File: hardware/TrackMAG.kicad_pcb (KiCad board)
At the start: 4 copper layers, 36 x 36 mm, 57 parts, among them J1 USB_C_Socket_USB2.0, J2 Conn_Debug, SW1 SW_RESET, SW2 SW_BOOT, SW3 SW_CALIBRATE, U1 LSM6DS3TR-C, U2 USBLC6-2P6, U3 STM32F103C8T6, U4 LIS2MDL, U5 AMS1117-3.3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

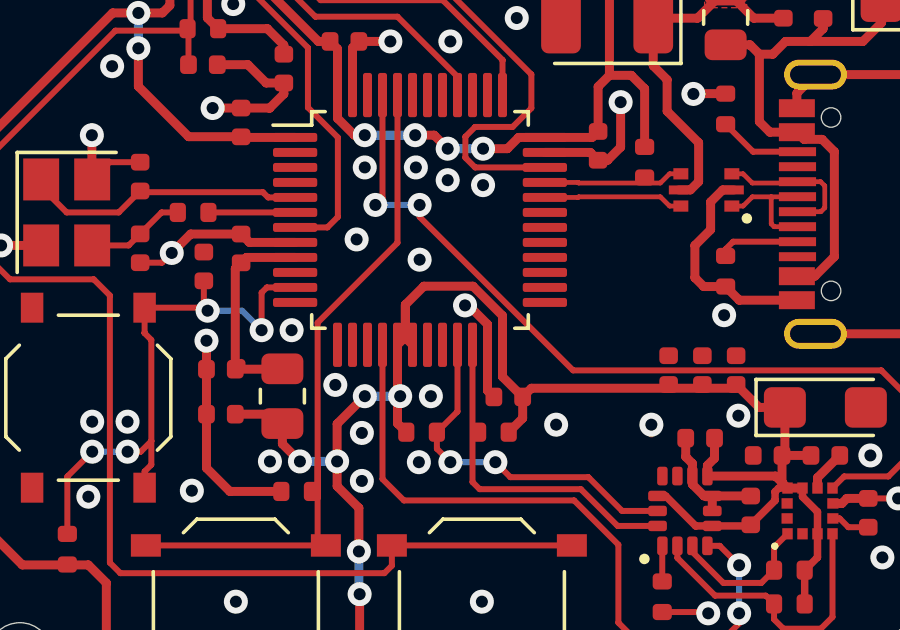
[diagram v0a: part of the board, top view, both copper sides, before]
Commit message: Remove redundant connection on PB0
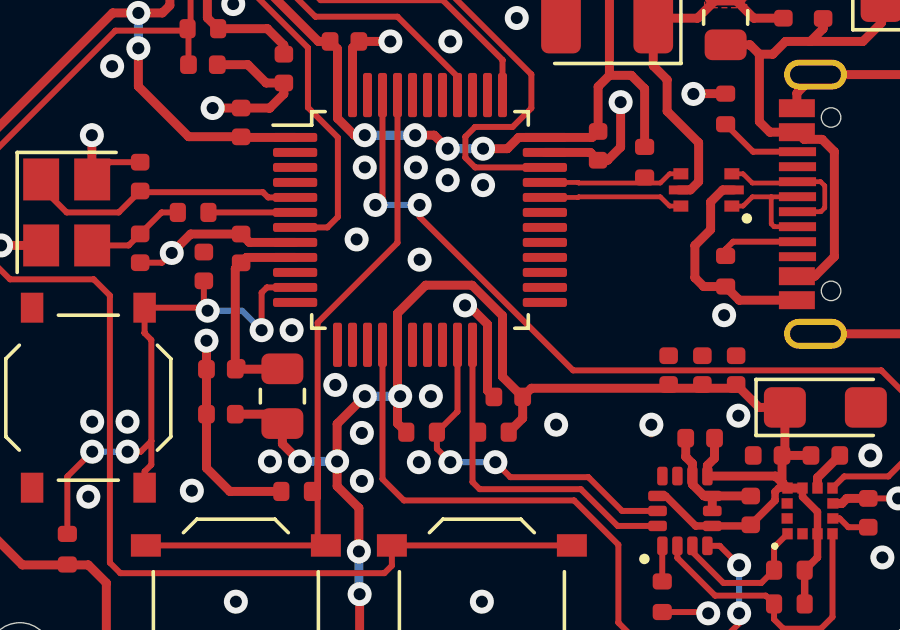
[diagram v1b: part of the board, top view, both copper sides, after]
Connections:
- U3 pad 18: +3.3V -> unconnected-(U3-PB0-Pad18)
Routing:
- net +3.3V: track 186.9 -> 185.5 mm
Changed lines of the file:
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@@
   (net 58 "/U_D+")
   (net 59 "/U_D-")
+  (net 60 "unconnected-(U3-PB0-Pad18)")
   (footprint "TrackMAG:C_0402_1005Metric" (layer "F.Cu")
     (at 148.725 97.375 180)
@@
       (net 1 "+3.3V") (pinfunction "PA7") (pintype "bidirectional"))
     (pad "18" smd roundrect (at -0.25 4.1625) (size 0.3 1.475) (layers "F.Cu" "F.Paste" "F.Mask") (roundrect_rratio 0.25)
-      (net 1 "+3.3V") (pinfunction "PB0") (pintype "bidirectional"))
+      (net 60 "unconnected-(U3-PB0-Pad18)") (pinfunction "PB0") (pintype "bidirectional+no_connect"))
     (pad "19" smd roundrect (at 0.25 4.1625) (size 0.3 1.475) (layers "F.Cu" "F.Paste" "F.Mask") (roundrect_rratio 0.25)
       (net 32 "unconnected-(U3-PB1-Pad19)") (pinfunction "PB1") (pintype "bidirectional+no_connect"))
@@
   (segment (start 127.675 71.675) (end 129.325 71.675) (width 0.3) (layer "F.Cu") (net 1))
   (segment (start 134.3875 83.8225) (end 134.14 83.575) (width 0.3) (layer "F.Cu") (net 1))
-  (segment (start 136.65 93.425) (end 136.3875 93.6875) (width 0.3) (layer "F.Cu") (net 1))
   (segment (start 146.955 97.47) (end 146.955 96.8) (width 0.3) (layer "F.Cu") (net 1))
   (segment (start 133.75 83.575) (end 129.325 79.15) (width 0.3) (layer "F.Cu") (net 1))
@@
   (segment (start 149.095 98.4625) (end 149.3875 98.4625) (width 0.25) (layer "F.Cu") (net 1))
   (segment (start 130.05 81.675) (end 130.05 82.79) (width 0.3) (layer "F.Cu") (net 1))
+  (segment (start 137.325 91.7) (end 138.870335 91.7) (width 0.3) (layer "F.Cu") (net 1))
   (segment (start 127.75 83.8045) (end 127.75 85.075) (width 0.3) (layer "F.Cu") (net 1))
   (segment (start 150.3875 99.9875) (end 150.3875 100.7725) (width 0.25) (layer "F.Cu") (net 1))
   (segment (start 146.88 99.725) (end 148.125 99.725) (width 0.25) (layer "F.Cu") (net 1))
   (segment (start 139.8875 93.6875) (end 139.8875 92.717165) (width 0.3) (layer "F.Cu") (net 1))
-  (segment (start 137.266685 91.733315) (end 136.65 92.35) (width 0.3) (layer "F.Cu") (net 1))
   (segment (start 141.3 86.775) (end 140.425 86.775) (width 0.3) (layer "F.Cu") (net 1))
-  (segment (start 139.8875 92.717165) (end 138.90365 91.733315) (width 0.3) (layer "F.Cu") (net 1))
+  (segment (start 138.870335 91.7) (end 139.8875 92.717165) (width 0.3) (layer "F.Cu") (net 1))
   (segment (start 127.75 82.625) (end 128.55 82.625) (width 0.3) (layer "F.Cu") (net 1))
   (segment (start 149.3 97.28) (end 149.205 97.375) (width 0.3) (layer "F.Cu") (net 1))
@@
   (segment (start 130.05 82.79) (end 130.41 83.15) (width 0.3) (layer "F.Cu") (net 1))
   (segment (start 143.4525 81.285) (end 140.7825 81.285) (width 0.3) (layer "F.Cu") (net 1))
+  (segment (start 136.3875 93.6875) (end 136.3875 92.6375) (width 0.3) (layer "F.Cu") (net 1))
   (segment (start 134.3875 86.1375) (end 134.949305 86.699305) (width 0.3) (layer "F.Cu") (net 1))
   (segment (start 134.85 104.125) (end 134 104.125) (width 0.3) (layer "F.Cu") (net 1))
@@
   (segment (start 146.7175 97.7075) (end 146.955 97.47) (width 0.3) (layer "F.Cu") (net 1))
   (segment (start 126.8305 72.5195) (end 127.675 71.675) (width 0.3) (layer "F.Cu") (net 1))
-  (segment (start 136.65 93.45) (end 136.8875 93.6875) (width 0.3) (layer "F.Cu") (net 1))
   (segment (start 148.44 95.775) (end 147.675 95.01) (width 0.3) (layer "F.Cu") (net 1))
   (segment (start 140.56 95.425) (end 140.56 96.135) (width 0.3) (layer "F.Cu") (net 1))
   (segment (start 150.3875 99.9875) (end 150.3875 99.255) (width 0.25) (layer "F.Cu") (net 1))
   (segment (start 149.205 97.375) (end 150.17 97.375) (width 0.3) (layer "F.Cu") (net 1))
-  (segment (start 136.65 92.35) (end 136.65 93.45) (width 0.3) (layer "F.Cu") (net 1))
   (segment (start 150.3875 99.255) (end 149.8875 98.755) (width 0.25) (layer "F.Cu") (net 1))
-  (segment (start 138.90365 91.733315) (end 137.266685 91.733315) (width 0.3) (layer "F.Cu") (net 1))
   (segment (start 132.05 83.15) (end 130.41 83.15) (width 0.3) (layer "F.Cu") (net 1))
   (segment (start 131.17 86.75) (end 131.175 86.755) (width 0.3) (layer "F.Cu") (net 1))
@@
   (segment (start 131.195 86.775) (end 131.175 86.755) (width 0.3) (layer "F.Cu") (net 1))
   (segment (start 149.3875 98.4625) (end 149.8875 98.4625) (width 0.3) (layer "F.Cu") (net 1))
-  (segment (start 136.65 92.35) (end 136.65 93.425) (width 0.3) (layer "F.Cu") (net 1))
   (segment (start 143.075 85.0825) (end 143.4525 84.705) (width 0.3) (layer "F.Cu") (net 1))
   (segment (start 127.75 82.625) (end 126.8925 82.625) (width 0.3) (layer "F.Cu") (net 1))
@@
   (segment (start 140.425 86.775) (end 140.05 87.15) (width 0.3) (layer "F.Cu") (net 1))
   (segment (start 140.05 87.15) (end 139.2395 87.15) (width 0.3) (layer "F.Cu") (net 1))
+  (segment (start 136.3875 92.6375) (end 137.325 91.7) (width 0.3) (layer "F.Cu") (net 1))
   (segment (start 132.2375 96) (end 132.55 96.3125) (width 0.3) (layer "F.Cu") (net 1))
   (segment (start 136.675 96.595) (end 136.68 96.6) (width 0.2) (layer "F.Cu") (net 1))

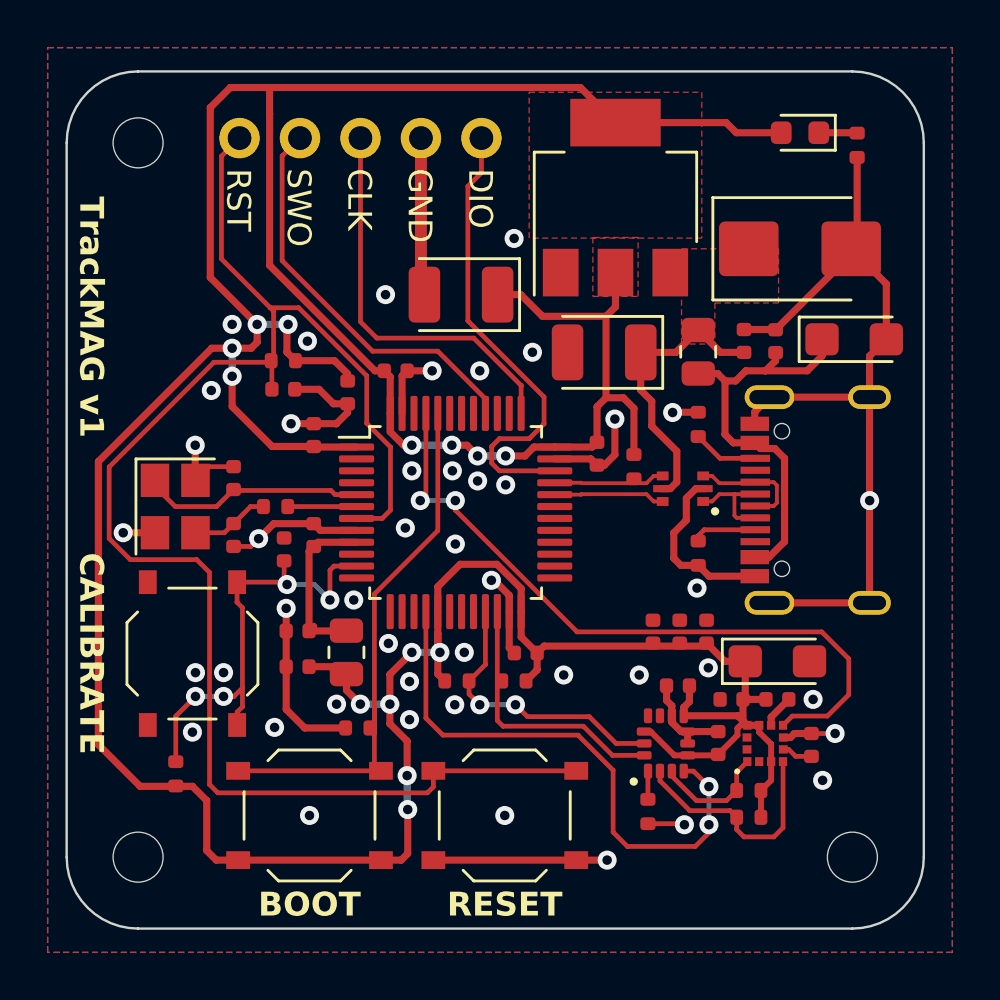
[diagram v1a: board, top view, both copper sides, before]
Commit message: Remove redundant vias, adjust reference vias
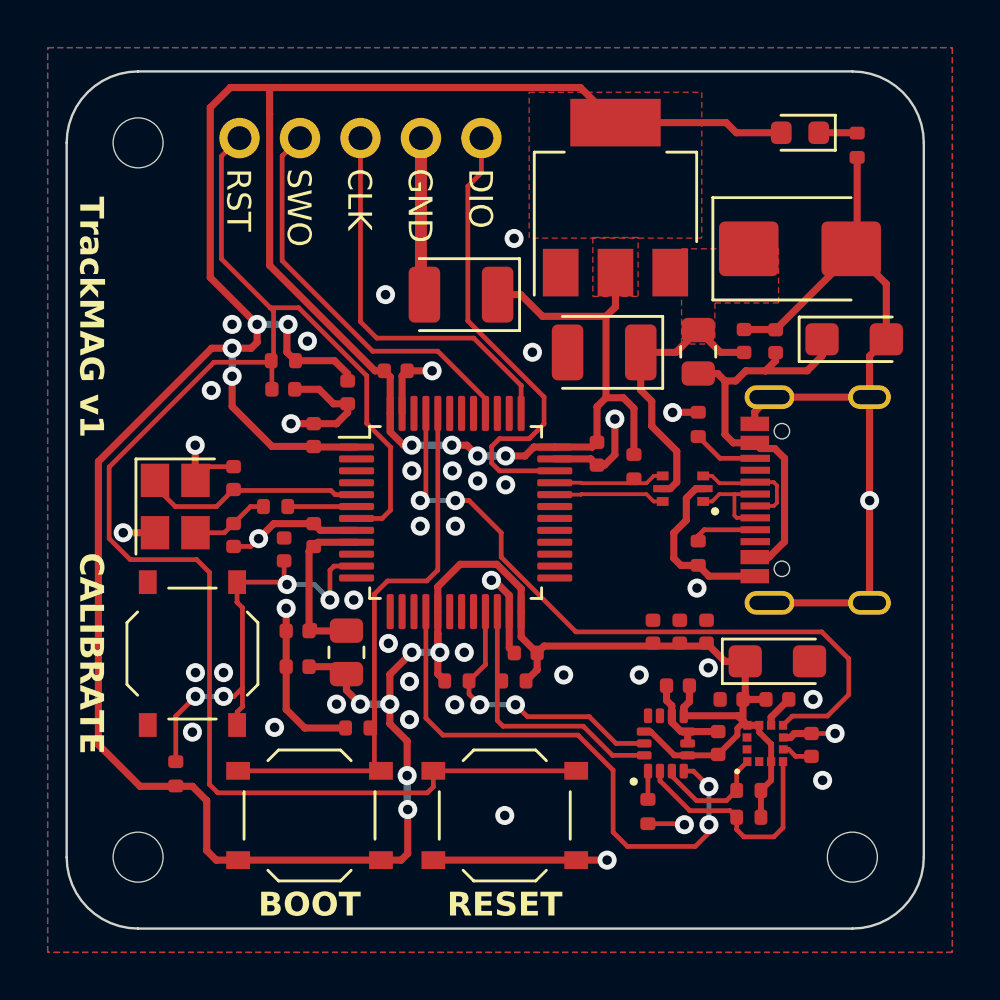
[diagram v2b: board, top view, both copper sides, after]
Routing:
- net /BOOT0: track 23.5 -> 24.5 mm
- net GND: vias 45 -> 43
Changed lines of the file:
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@@
   (via (at 152.15 97.375) (size 0.8) (drill 0.4) (layers "F.Cu" "B.Cu") (net 2))
   (via (at 134.1925 80.375) (size 0.8) (drill 0.4) (layers "F.Cu" "B.Cu") (free) (net 2))
-  (via (at 138.15 83.575) (size 0.8) (drill 0.4) (layers "F.Cu" "B.Cu") (free) (net 2))
   (via (at 135.296271 87.775) (size 0.8) (drill 0.4) (layers "F.Cu" "B.Cu") (free) (net 2))
   (via (at 147.75 96.05) (size 0.8) (drill 0.4) (layers "F.Cu" "B.Cu") (free) (net 2))
@@
   (via (at 137 87.775) (size 0.8) (drill 0.4) (layers "F.Cu" "B.Cu") (free) (net 2))
   (via (at 154.525 89.025) (size 0.8) (drill 0.4) (layers "F.Cu" "B.Cu") (net 2))
-  (via (at 137.125 90.85) (size 0.8) (drill 0.4) (layers "F.Cu" "B.Cu") (free) (net 2))
+  (via (at 137.125 90.1) (size 0.8) (drill 0.4) (layers "F.Cu" "B.Cu") (free) (net 2))
   (via (at 126.2 86.7) (size 0.8) (drill 0.4) (layers "F.Cu" "B.Cu") (net 2))
   (via (at 136.15 83.575) (size 0.8) (drill 0.4) (layers "F.Cu" "B.Cu") (net 2))
@@
   (via (at 146.745 102.6375) (size 0.8) (drill 0.4) (layers "F.Cu" "B.Cu") (net 2))
   (via (at 129.5325 98.55) (size 0.8) (drill 0.4) (layers "F.Cu" "B.Cu") (free) (net 2))
-  (via (at 131 102.25) (size 0.8) (drill 0.4) (layers "F.Cu" "B.Cu") (free) (net 2))
   (via (at 139.2395 88.3645) (size 0.8) (drill 0.4) (layers "F.Cu" "B.Cu") (free) (net 2))
   (via (at 123.175 90.375) (size 0.8) (drill 0.4) (layers "F.Cu" "B.Cu") (net 2))
   (via (at 153.075 98.8075) (size 0.8) (drill 0.4) (layers "F.Cu" "B.Cu") (net 2))
   (via (at 126.2105 96.250497) (size 0.8) (drill 0.4) (layers "F.Cu" "B.Cu") (free) (net 2))
-  (via (at 135.025 90.175) (size 0.8) (drill 0.4) (layers "F.Cu" "B.Cu") (free) (net 2))
+  (via (at 135.65 90.1) (size 0.8) (drill 0.4) (layers "F.Cu" "B.Cu") (free) (net 2))
   (via (at 130.912196 82.328872) (size 0.8) (drill 0.4) (layers "F.Cu" "B.Cu") (free) (net 2))
   (via (at 141.675 96.35) (size 0.8) (drill 0.4) (layers "F.Cu" "B.Cu") (free) (net 2))
@@
   (segment (start 145.2125 101.575) (end 145.2125 100.3925) (width 0.2) (layer "F.Cu") (net 13))
   (segment (start 145.2125 100.3925) (end 145.2175 100.3875) (width 0.2) (layer "F.Cu") (net 13))
+  (segment (start 134.275 92.4) (end 133.725 92.95) (width 0.2) (layer "F.Cu") (net 14))
   (segment (start 133.7245 100.0995) (end 133.7245 97.525) (width 0.2) (layer "F.Cu") (net 14))
   (segment (start 134.2 100.375) (end 128.2 100.375) (width 0.2) (layer "F.Cu") (net 14))
   (segment (start 134 100.375) (end 133.7245 100.0995) (width 0.2) (layer "F.Cu") (net 14))
-  (segment (start 136.3875 90.2875) (end 133.725 92.95) (width 0.2) (layer "F.Cu") (net 14))
+  (segment (start 136.3875 85.3625) (end 136.3875 91.9375) (width 0.2) (layer "F.Cu") (net 14))
   (segment (start 133.725 92.95) (end 133.725 98.8) (width 0.2) (layer "F.Cu") (net 14))
-  (segment (start 136.3875 85.3625) (end 136.3875 90.2875) (width 0.2) (layer "F.Cu") (net 14))
+  (segment (start 135.925 92.4) (end 134.275 92.4) (width 0.2) (layer "F.Cu") (net 14))
+  (segment (start 136.3875 91.9375) (end 135.925 92.4) (width 0.2) (layer "F.Cu") (net 14))
   (segment (start 126.21 90.375) (end 127.425 90.375) (width 0.2) (layer "F.Cu") (net 15))
   (segment (start 128.525 89.275) (end 127.81 89.99) (width 0.2) (layer "F.Cu") (net 15))
@@
   (segment (start 130.0575 92.55) (end 131.207997 92.55) (width 0.2) (layer "B.Cu") (net 27))
   (segment (start 126.2105 97.25) (end 127.3895 97.25) (width 0.2) (layer "B.Cu") (net 27))
-  (segment (start 142.24 94.54) (end 137.125 89.425) (width 0.2) (layer "F.Cu") (net 45))
+  (segment (start 137.7 89.025) (end 139.05 90.375) (width 0.2) (layer "F.Cu") (net 45))
+  (segment (start 153.65 95.675) (end 153.65 97.175) (width 0.2) (layer "F.Cu") (net 45))
   (segment (start 137.125 89.025) (end 137.125 89.15) (width 0.2) (layer "F.Cu") (net 45))
   (segment (start 135.8875 85.3625) (end 135.875 85.375) (width 0.2) (layer "F.Cu") (net 45))
-  (segment (start 153.65 97.175) (end 153.65 95.675) (width 0.2) (layer "F.Cu") (net 45))
-  (segment (start 153.65 95.675) (end 152.515 94.54) (width 0.2) (layer "F.Cu") (net 45))
-  (segment (start 152.515 94.54) (end 142.24 94.54) (width 0.2) (layer "F.Cu") (net 45))
-  (segment (start 150.8875 98.4625) (end 151.275 98.075) (width 0.2) (layer "F.Cu") (net 45))
+  (segment (start 139.05 90.375) (end 139.05 91.398833) (width 0.2) (layer "F.Cu") (net 45))
+  (segment (start 153.65 97.175) (end 152.75 98.075) (width 0.2) (layer "F.Cu") (net 45))
+  (segment (start 152.515 94.54) (end 153.65 95.675) (width 0.2) (layer "F.Cu") (net 45))
   (segment (start 135.8875 85.3625) (end 135.8875 88.7875) (width 0.2) (layer "F.Cu") (net 45))
   (segment (start 135.8875 88.7875) (end 135.65 89.025) (width 0.2) (layer "F.Cu") (net 45))
   (segment (start 135.875 85.375) (end 135.85 85.375) (width 0.2) (layer "F.Cu") (net 45))
-  (segment (start 137.125 89.425) (end 137.125 89.025) (width 0.2) (layer "F.Cu") (net 45))
+  (segment (start 152.75 98.075) (end 151.275 98.075) (width 0.2) (layer "F.Cu") (net 45))
+  (segment (start 151.275 98.075) (end 150.8875 98.4625) (width 0.2) (layer "F.Cu") (net 45))
   (segment (start 137.125 89.15) (end 137.1 89.175) (width 0.2) (layer "F.Cu") (net 45))
-  (segment (start 152.75 98.075) (end 153.65 97.175) (width 0.2) (layer "F.Cu") (net 45))
-  (segment (start 151.275 98.075) (end 152.75 98.075) (width 0.2) (layer "F.Cu") (net 45))
+  (segment (start 139.05 91.398833) (end 142.191167 94.54) (width 0.2) (layer "F.Cu") (net 45))
+  (segment (start 137.125 89.025) (end 137.7 89.025) (width 0.2) (layer "F.Cu") (net 45))
+  (segment (start 142.191167 94.54) (end 152.515 94.54) (width 0.2) (layer "F.Cu") (net 45))
   (via (at 135.65 89.025) (size 0.8) (drill 0.4) (layers "F.Cu" "B.Cu") (net 45))
   (via (at 137.125 89.025) (size 0.8) (drill 0.4) (layers "F.Cu" "B.Cu") (net 45))

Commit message: Optimize PCB layout
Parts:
- added H4: MountingHole, MountingHole:MountingHole_2.1mm, F.Cu at (153.8, 74.0)
- moved D1 38.2 mm to (128.5, 104.0), turned to 90 degrees
- moved R13 38.0 mm to (130.5, 104.0), turned to 90 degrees
- moved SW2 20.5 mm to (126.0, 82.4), turned to 90 degrees
- moved R7 15.8 mm to (132.1, 82.8)
- moved SW1 14.3 mm to (126.0, 96.9), turned to 90 degrees
- moved R12 11.8 mm to (136.9, 98.2), turned to 0 degrees
- moved SW3 11.5 mm to (135.7, 101.8), turned to 180 degrees
- moved R1 9.19 mm to (129.4, 92.3)
- moved C23 8.76 mm to (134.9, 98.2), turned to 180 degrees
- moved C17 6.87 mm to (129.4, 91.2)
- moved C15 1.85 mm to (130.5, 96.3)
- moved C16 1.50 mm to (130.5, 94.5)
- moved C3 1.31 mm to (144.2, 94.8)
- moved C1 1.29 mm to (146.4, 94.8)
- moved C2 1.29 mm to (145.3, 94.8)
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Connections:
- U3 pad 11: CALIBRATE -> unconnected-(U3-PA1-Pad11)
- U3 pad 15: unconnected-(U3-PA5-Pad15) -> CALIBRATE
- U3 pad 16: INT1 -> unconnected-(U3-PA6-Pad16)
- U3 pad 17: +3.3V -> unconnected-(U3-PA7-Pad17)
- U3 pad 26: unconnected-(U3-PB13-Pad26) -> DRDY
- U3 pad 27: unconnected-(U3-PB14-Pad27) -> INT1
- U3 pad 45: DRDY -> unconnected-(U3-PB8-Pad45)
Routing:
- net +3.3V: track 185.5 -> 121.9 mm, vias 14 -> 2
- net GND: track 101.8 -> 72.8 mm, vias 43 -> 25
- net RESET: track 66.4 -> 40.3 mm
- net DRDY: track 30.1 -> 18.4 mm, vias 2 -> 0
- net +3.3VA: track 7.35 -> 16.9 mm
- net CALIBRATE: track 19.1 -> 12.0 mm, vias 4 -> 2
- net INT1: track 23.6 -> 29.5 mm
- net /BOOT0: track 24.5 -> 18.7 mm
- net I2C2_SCL: track 12.1 -> 10.8 mm, vias 2 -> 0
- net I2C2_SDA: track 11.3 -> 10.7 mm, vias 0 -> 2
- net /HSE_IN: track 9.55 -> 10.2 mm
- net /HSE_O: track 2.89 -> 3.43 mm
